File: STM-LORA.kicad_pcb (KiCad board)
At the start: 2 copper layers, 56.5 x 50.8 mm, 22 parts, among them J1 Batt, J11 CONN_02X09, J13 CONN_01X02, J2 Solar, J3 CONN_01X17, J4 CONN_01X03, J6 CONN_01X01, J9 CONN_01X05, U1 stm32f103c8t6-module-china, U2 RFM95HW

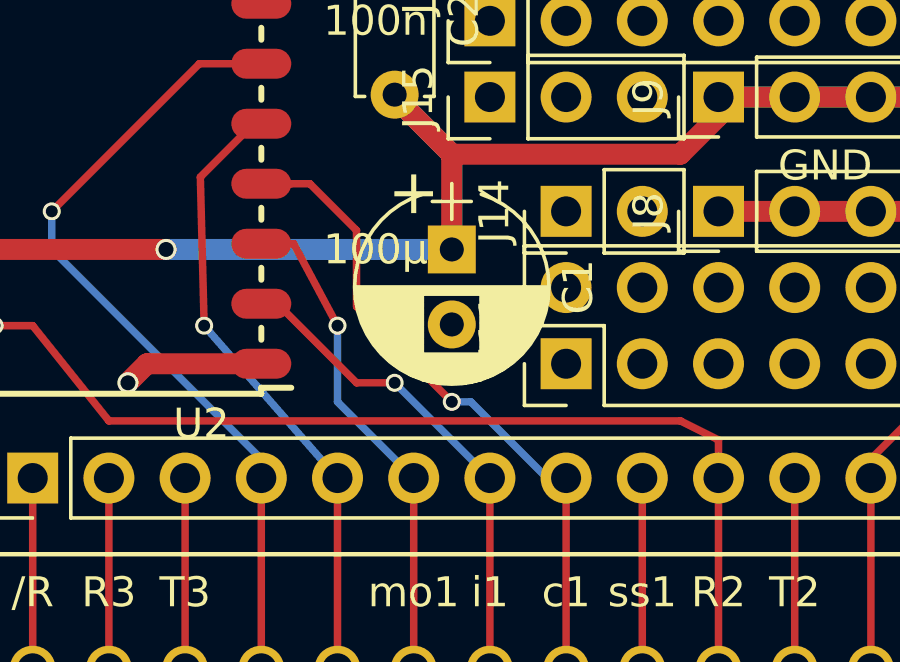
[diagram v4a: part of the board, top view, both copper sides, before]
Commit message: reposition capacitor
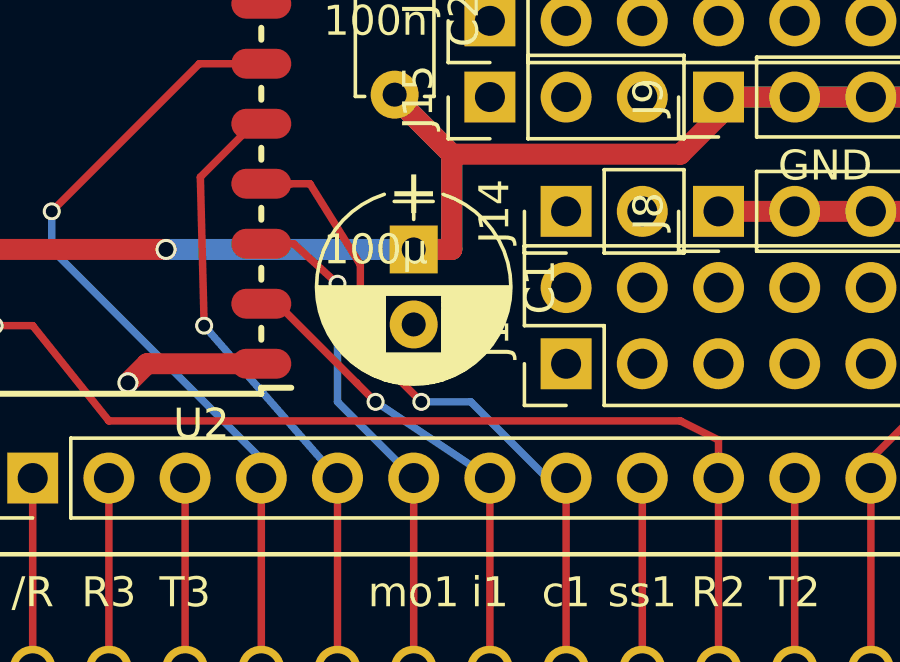
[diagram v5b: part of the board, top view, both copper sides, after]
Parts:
- moved C1 1.27 mm to (108.0, 68.6)
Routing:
- net /3V3: track 180.8 -> 182.0 mm
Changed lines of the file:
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@@
     (links 75)
     (no_connects 0)
-    (area 83.744999 55.315 141.390371 109.173333)
+    (area 83.744999 55.804999 140.410001 106.755001)
     (thickness 1.6)
     (drawings 20)
-    (tracks 165)
+    (tracks 166)
     (zones 0)
     (modules 22)
@@
     (aux_axis_origin 0 0)
     (grid_origin 83.82 55.88)
-    (visible_elements 7FFFFFFF)
+    (visible_elements 7FFFBFFF)
     (pcbplotparams
       (layerselection 0x010e0_80000001)
@@
   )
   (module Capacitors_THT:CP_Radial_D6.3mm_P2.50mm (layer F.Cu)
-    (at 109.22 68.58 270)
+    (at 107.95 68.58 270)
     (descr "CP, Radial series, Radial, pin pitch=2.50mm, , diameter=6.3mm, Electrolytic Capacitor")
     (tags "CP Radial series Radial pin pitch 2.50mm  diameter 6.3mm Electrolytic Capacitor")
@@
   (segment (start 90.17 97.79) (end 90.17 104.14) (width 0.25) (layer F.Cu) (net 25) (status 30))
   (segment (start 87.63 104.14) (end 87.63 97.79) (width 0.25) (layer F.Cu) (net 26) (status 30))
+  (segment (start 109.22 68.58) (end 107.95 68.58) (width 0.7) (layer F.Cu) (net 27))
   (segment (start 128.27 63.5) (end 128.27 65.405) (width 0.7) (layer F.Cu) (net 27) (status 10))
   (segment (start 137.795 96.52) (end 136.525 97.79) (width 0.7) (layer F.Cu) (net 27) (status 20))
@@
   (segment (start 107.95 76.2) (end 105.41 73.66) (width 0.25) (layer B.Cu) (net 34) (status 10))
   (segment (start 103.95 68.39) (end 102.87 68.39) (width 0.25) (layer F.Cu) (net 34) (status 20))
-  (segment (start 105.41 71.12) (end 103.95 68.39) (width 0.25) (layer F.Cu) (net 34))
-  (via (at 105.41 71.12) (size 0.6) (drill 0.4) (layers F.Cu B.Cu) (net 34))
-  (segment (start 105.41 73.66) (end 105.41 71.12) (width 0.25) (layer B.Cu) (net 34))
+  (segment (start 105.41 69.723) (end 103.95 68.39) (width 0.25) (layer F.Cu) (net 34))
+  (via (at 105.41 69.723) (size 0.6) (drill 0.4) (layers F.Cu B.Cu) (net 34))
+  (segment (start 105.41 73.66) (end 105.41 69.723) (width 0.25) (layer B.Cu) (net 34))
   (segment (start 107.95 82.55) (end 107.95 76.2) (width 0.25) (layer F.Cu) (net 34) (status 30))
-  (segment (start 107.315 73.025) (end 106.045 73.025) (width 0.25) (layer F.Cu) (net 35))
+  (segment (start 106.68 73.66) (end 106.045 73.025) (width 0.25) (layer F.Cu) (net 35))
   (segment (start 106.045 73.025) (end 103.4575 70.4375) (width 0.25) (layer F.Cu) (net 35) (status 20))
-  (segment (start 110.49 76.2) (end 107.315 73.025) (width 0.25) (layer B.Cu) (net 35) (status 10))
-  (via (at 107.315 73.025) (size 0.6) (drill 0.4) (layers F.Cu B.Cu) (net 35))
+  (segment (start 110.49 76.2) (end 106.68 73.66) (width 0.25) (layer B.Cu) (net 35) (status 10))
+  (via (at 106.68 73.66) (size 0.6) (drill 0.4) (layers F.Cu B.Cu) (net 35))
   (via (at 110.49 76.2) (size 0.6) (drill 0.4) (layers F.Cu B.Cu) (net 35) (status 30))
   (segment (start 110.49 82.55) (end 110.49 76.2) (width 0.25) (layer F.Cu) (net 35) (status 30))
@@
   (segment (start 112.395 76.2) (end 109.855 73.66) (width 0.25) (layer B.Cu) (net 36) (status 10))
   (segment (start 104.49 66.39) (end 102.87 66.39) (width 0.25) (layer F.Cu) (net 36) (status 20))
-  (segment (start 106.045 67.945) (end 104.49 66.39) (width 0.25) (layer F.Cu) (net 36))
-  (segment (start 106.045 70.485) (end 106.045 67.945) (width 0.25) (layer F.Cu) (net 36))
-  (segment (start 109.22 73.66) (end 106.045 70.485) (width 0.25) (layer F.Cu) (net 36))
-  (via (at 109.22 73.66) (size 0.6) (drill 0.4) (layers F.Cu B.Cu) (net 36))
-  (segment (start 109.855 73.66) (end 109.22 73.66) (width 0.25) (layer B.Cu) (net 36))
+  (segment (start 106.172 69.088) (end 104.49 66.39) (width 0.25) (layer F.Cu) (net 36))
+  (segment (start 106.172 71.628) (end 106.172 69.088) (width 0.25) (layer F.Cu) (net 36))
+  (segment (start 108.204 73.66) (end 106.172 71.628) (width 0.25) (layer F.Cu) (net 36))
+  (via (at 108.204 73.66) (size 0.6) (drill 0.4) (layers F.Cu B.Cu) (net 36))
+  (segment (start 109.855 73.66) (end 108.204 73.66) (width 0.25) (layer B.Cu) (net 36))
   (via (at 113.03 76.2) (size 0.6) (drill 0.4) (layers F.Cu B.Cu) (net 36) (status 30))
   (segment (start 103.855 66.39) (end 102.87 66.39) (width 0.25) (layer F.Cu) (net 36) (status 30))

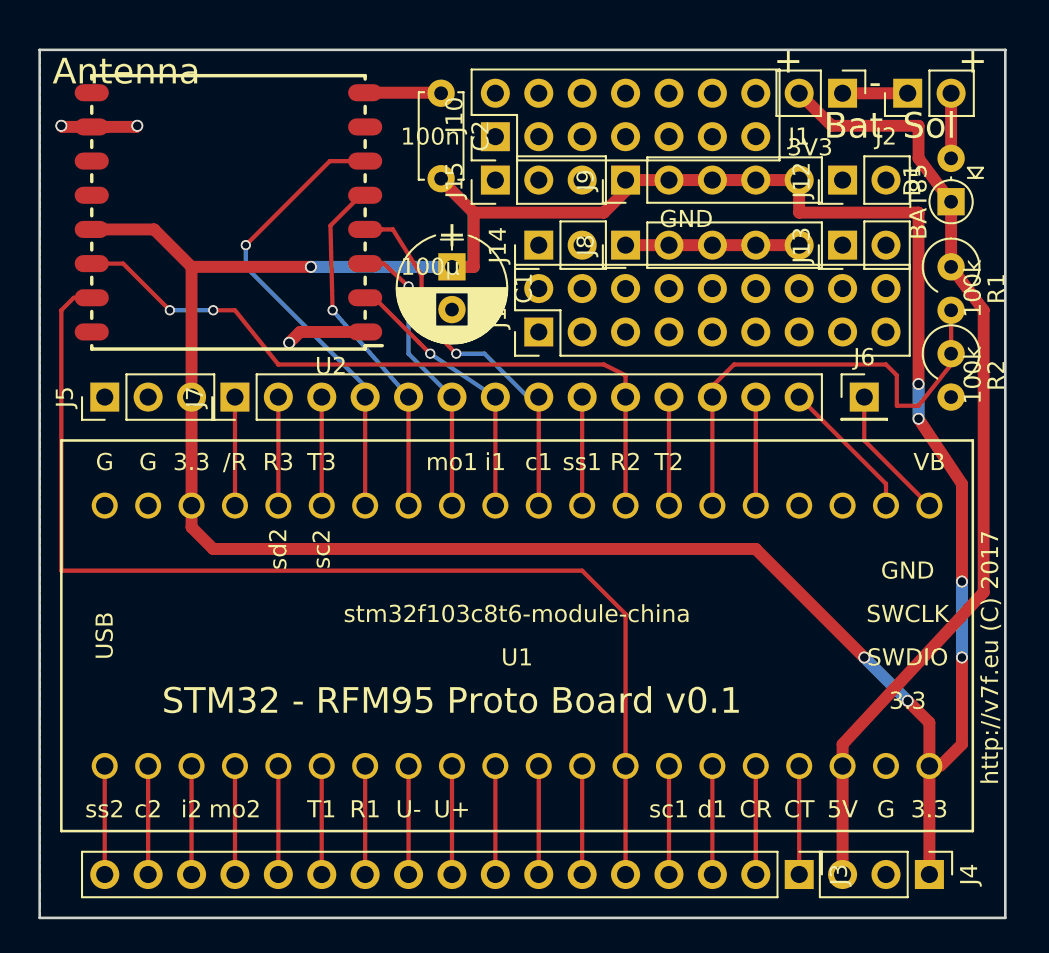
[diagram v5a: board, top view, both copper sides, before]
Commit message: Layout silk screen
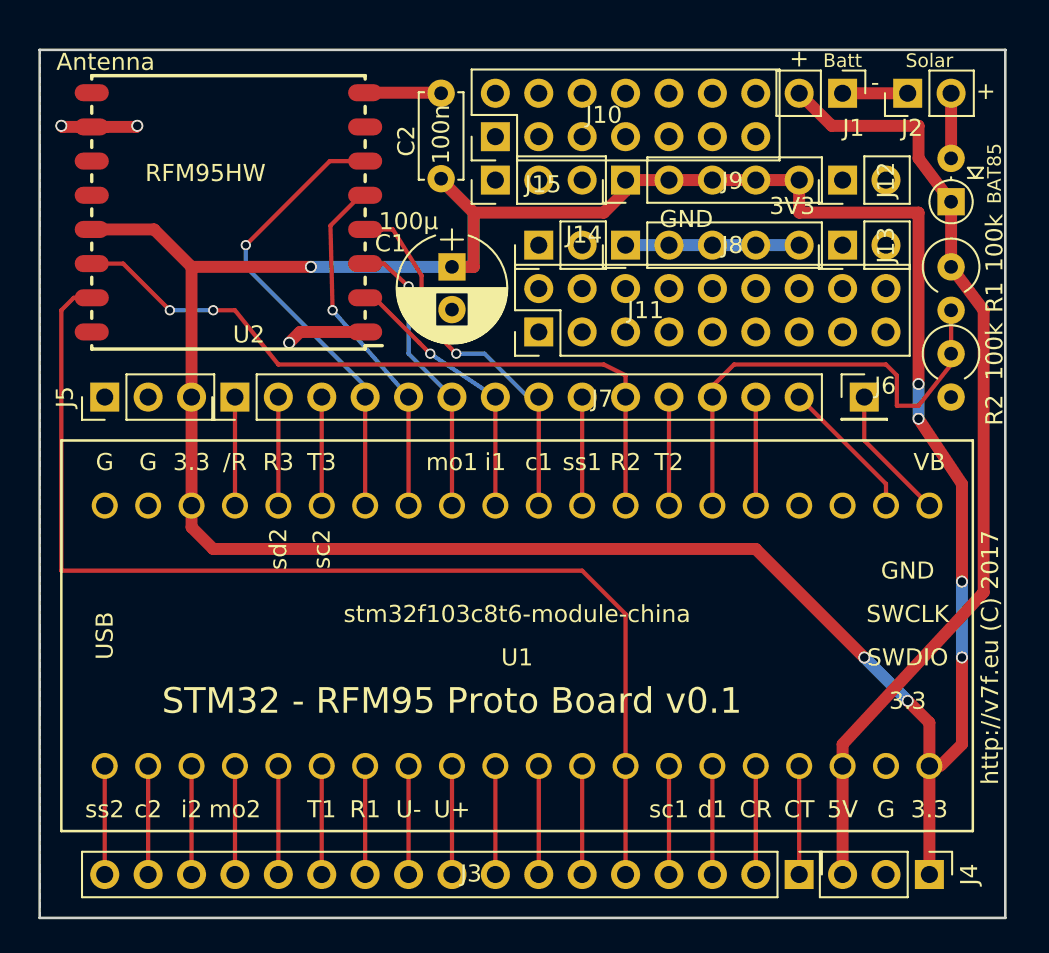
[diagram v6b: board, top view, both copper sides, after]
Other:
- board text removed: "100k"
- board text removed: "100n"
- board text removed: "100µ"
- board text removed: "BAT85"
- board text removed: "Bat"
- board text removed: "Sol"

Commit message: layout silk screen
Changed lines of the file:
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@@
-(kicad_pcb (version 4) (host pcbnew 4.0.6)
+(kicad_pcb (version 4) (host pcbnew 4.0.6-e0-6349~53~ubuntu16.04.1)
   (general
     (links 75)
     (no_connects 0)
-    (area 83.744999 55.563 140.775 109.173333)
+    (area 83.744999 55.804999 140.410001 106.755001)
     (thickness 1.6)
     (drawings 12)
@@
     (descr "CP, Radial series, Radial, pin pitch=2.50mm, , diameter=6.3mm, Electrolytic Capacitor")
     (tags "CP Radial series Radial pin pitch 2.50mm  diameter 6.3mm Electrolytic Capacitor")
-    (fp_text reference C1 (at -1.3716 3.6068 360) (layer F.SilkS)
-      (effects (font (size 1 1) (thickness 0.15)))
-    )
-    (fp_text value 100µ (at -2.667 2.54 360) (layer F.SilkS)
+    (fp_text reference C1 (at 0.254 1.905 360) (layer F.SilkS)
+      (effects (font (size 1 1) (thickness 0.15)))
+    )
+    (fp_text value 100µ (at -2.921 1.778 360) (layer F.SilkS)
       (effects (font (size 1 1) (thickness 0.15)))
     )
@@
     (effects (font (size 1 1) (thickness 0.2)))
   )
-  (segment (start 128.27 67.31) (end 118.11 67.31) (width 0.7) (layer B.Cu) (net 8) (status C00000))
+  (segment (start 128.27 67.31) (end 118.11 67.31) (width 0.7) (layer B.Cu) (net 8))
   (segment (start 130.81 58.42) (end 134.62 58.42) (width 0.7) (layer F.Cu) (net 8) (status 30))
   (segment (start 86.87 60.39) (end 85.155 60.39) (width 0.7) (layer F.Cu) (net 8) (status 10))
